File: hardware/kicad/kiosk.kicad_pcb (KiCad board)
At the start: 2 copper layers, 178 x 116 mm, 15 parts, among them J10 TerminalBlock_MaiXu_MX126-5.0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, J11 TerminalBlock_MaiXu_MX126-5.0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, J13 PinSocket_1x09_P2.54mm_Vertic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, J3 PinSocket_1x14_P2.54mm_Vertic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, J4 PinSocket_1x06_P2.54mm_Vertic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, J5 PinHeader_1x04_P2.54mm_Vertic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, J6 PinSocket_1x06_P2.54mm_Vertic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, J7 PinSocket_1x07_P2.54mm_Vertic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, J9 PinHeader_1x03_P2.54mm_Vertic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, U1 ESP32-S3-CAM

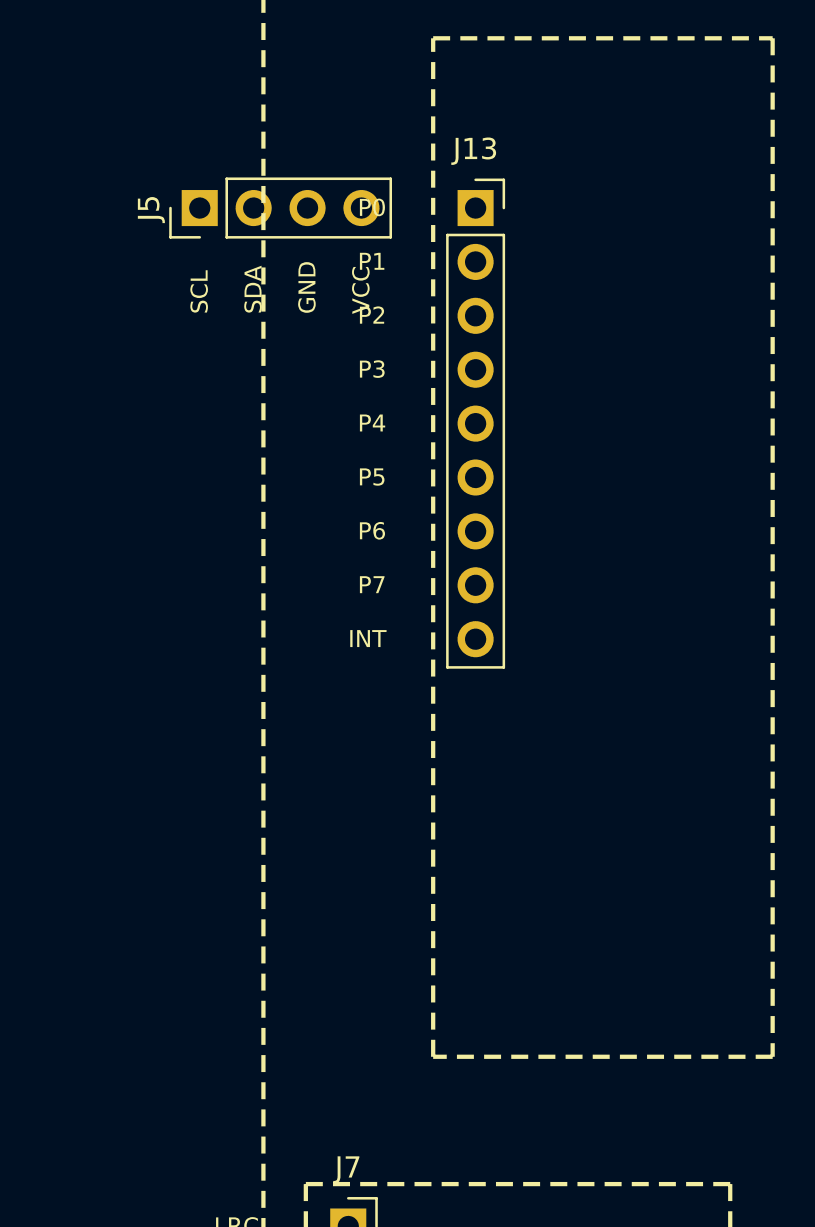
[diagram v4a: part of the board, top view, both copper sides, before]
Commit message: fix(hardware): put the expander's socket and wire holes back the right way
I swapped them last commit on my own reasoning about which row holds the
module better, against what had already been decided: the four supply
pins are soldered pointing down and seat in J5; the port row stays
pointing up and takes wire, stripped and soldered into J13.

J13 keeps all nine holes even though three carry a signal. The six spare
ones cost nothing now and save cutting the board later.

J13 also moves into the gap between the panel and the module, where it
was overlapping the panel's area.
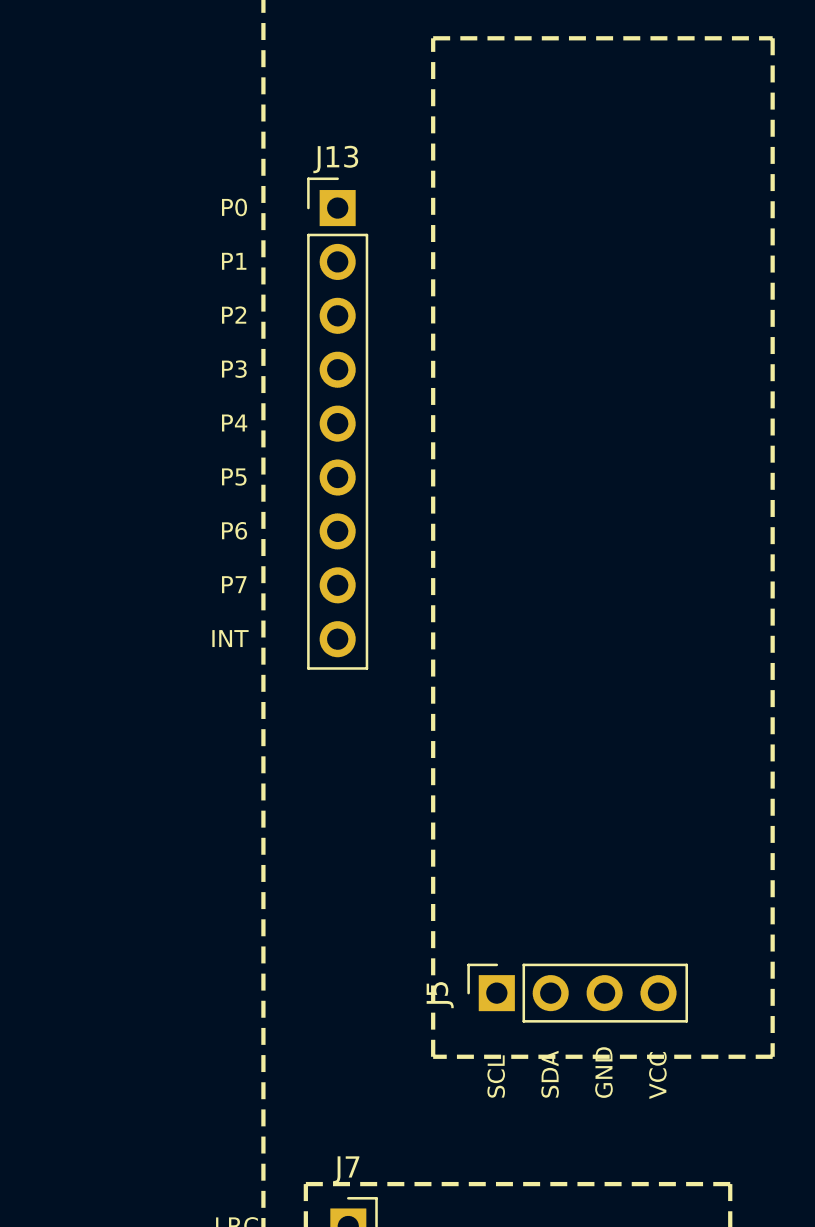
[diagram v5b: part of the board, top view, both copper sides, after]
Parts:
- J13: value PinSocket_1x09_P2.54mm_Vertical -> PinHeader_1x09_P2.54mm_Vertical; footprint Connector_PinSocket_2.54mm:PinSocket_1x09_P2.54mm_Vertical -> Connector_PinHeader_2.54mm:PinHeader_1x09_P2.54mm_Vertical
- J5: value PinHeader_1x04_P2.54mm_Vertical -> PinSocket_1x04_P2.54mm_Vertical; footprint Connector_PinHeader_2.54mm:PinHeader_1x04_P2.54mm_Vertical -> Connector_PinSocket_2.54mm:PinSocket_1x04_P2.54mm_Vertical
- moved J5 39.6 mm to (115.0, 51.0)
- moved J13 6.50 mm to (107.5, 14.0)

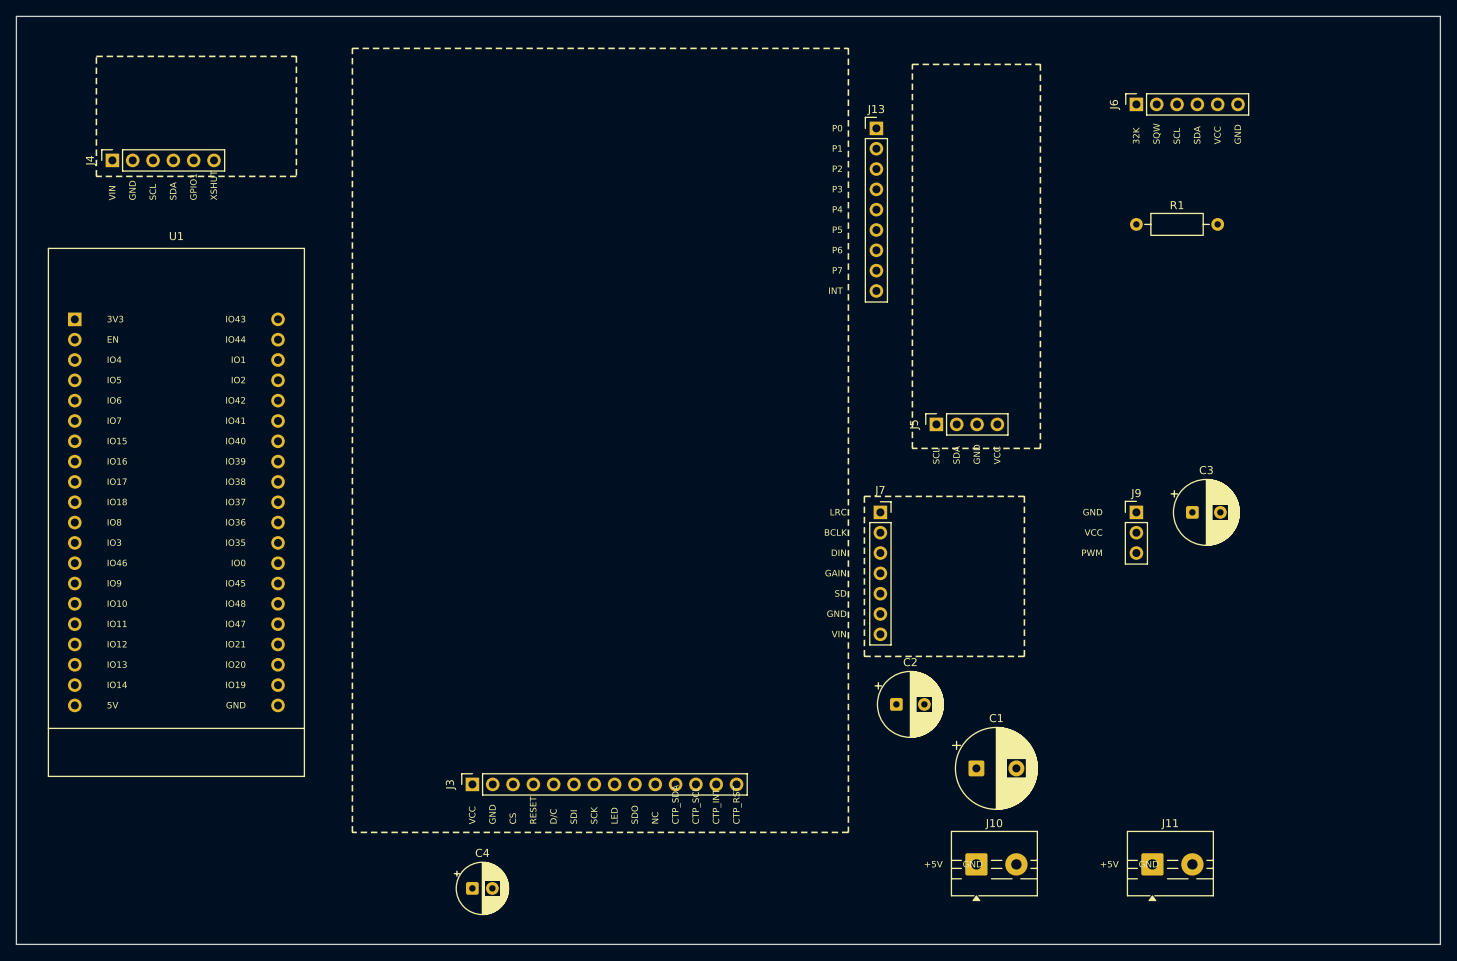
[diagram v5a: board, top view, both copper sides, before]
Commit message: refactor(hardware): square the layout into bands and take back the slack
Parts had been nudged one at a time to clear whatever they last collided
with, and it showed: nothing lined up with anything and the right side had
gaps that were only there because no part had been dropped in them.

Right of the panel is now three bands. The I2C parts above y=54, the two
switching loads between 58 and 80 with a capacitor each, the bulk
capacitor and the two supply terminals below 84. J7 moves to the right
edge of the amplifier's outline so C2 can sit beside it - from the left
edge it was 28 mm away with the module's own body in between.

170 by 116, eight millimetres narrower, with nothing off the board and no
part inside a module's outline.
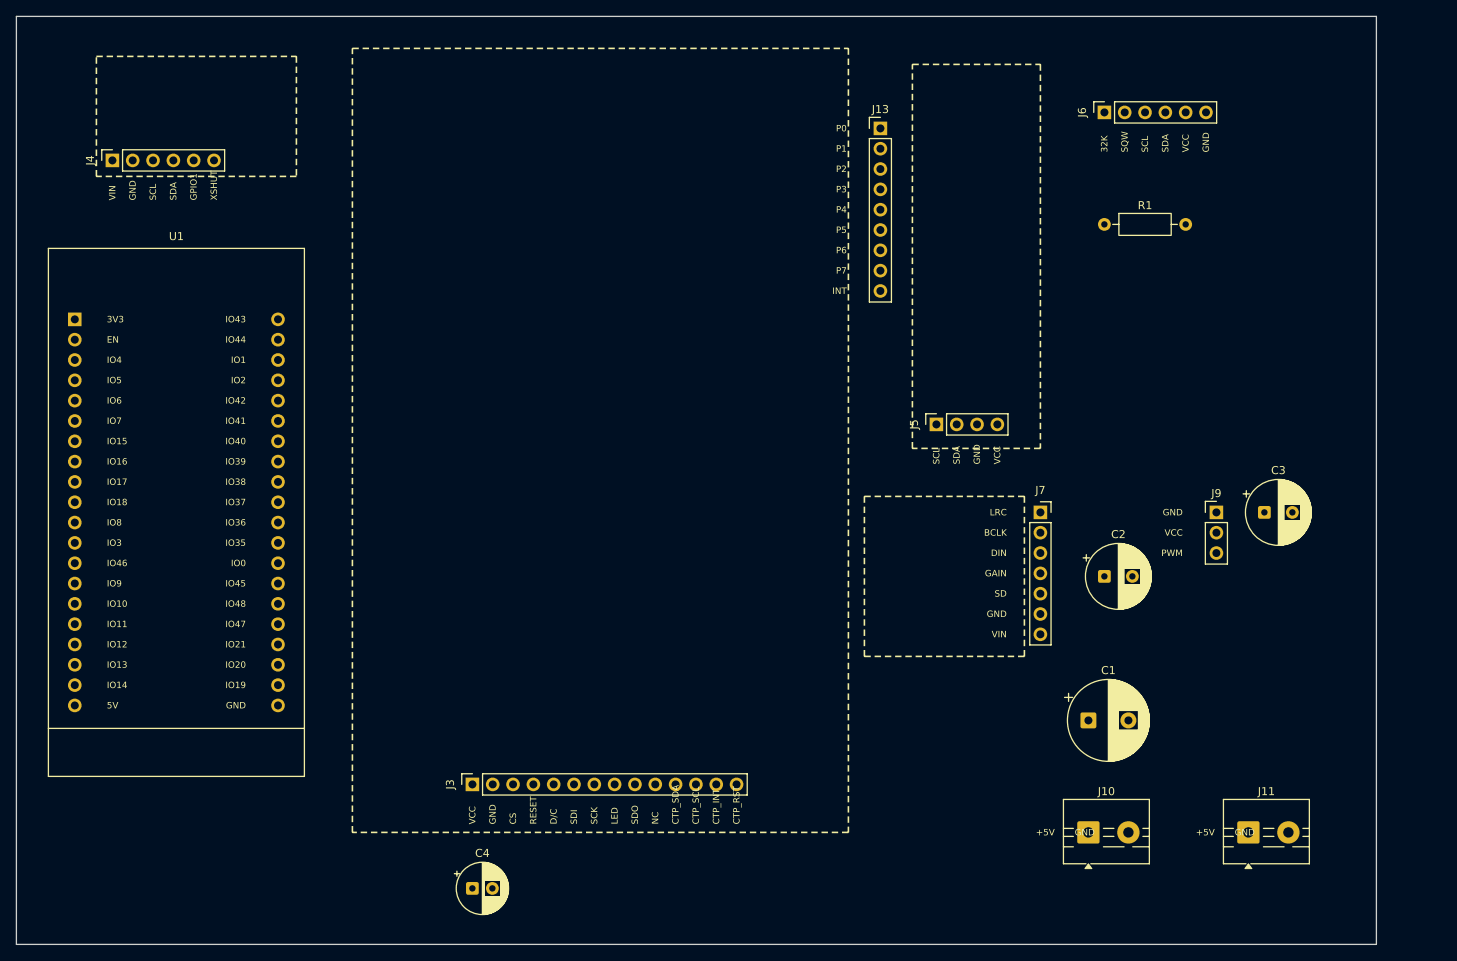
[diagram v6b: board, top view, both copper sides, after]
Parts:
- moved C2 30.5 mm to (136.0, 70.0)
- moved J7 20.0 mm to (128.0, 62.0)
- moved C1 15.2 mm to (134.0, 88.0)
- moved J10 14.6 mm to (134.0, 102.0)
- moved J11 12.6 mm to (154.0, 102.0)
- moved J9 10.0 mm to (150.0, 62.0)
- moved C3 9.00 mm to (156.0, 62.0)
- moved J6 4.12 mm to (136.0, 12.0)
- moved R1 4.00 mm to (136.0, 26.0)
- moved J13 0.50 mm to (108.0, 14.0)
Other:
- board size 178 x 116 mm -> 170 x 116 mm
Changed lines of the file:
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@@
 	(footprint "Connector_PinSocket_2.54mm:PinSocket_1x07_P2.54mm_Vertical"
 		(layer "F.Cu")
-		(at 108 62)
+		(at 128 62)
 		(descr "Through hole straight socket strip, 1x07, 2.54mm pitch, single row (from Kicad 4.0.7), script generated")
 		(tags "Through hole socket strip THT 1x07 2.54mm single row")
@@
 	(footprint "TerminalBlock:TerminalBlock_MaiXu_MX126-5.0-02P_1x02_P5.00mm"
 		(layer "F.Cu")
-		(at 142 106)
+		(at 154 102)
 		(descr "terminal block MaiXu MX126-5.0-02P, 2 pins, pitch 5mm, size 10.5x7.8mm, drill diameter 1.3mm, pad diameter 2.8mm, https://www.lcsc.com/datasheet/lcsc_datasheet_2309150913_MAX-MX126-5-0-03P-GN01-Cu-S-A_C5188435.pdf")
 		(tags "THT terminal block MaiXu MX126-5.0-02P pitch 5mm size 10.5x7.8mm drill 1.3mm pad 2.8mm")
@@
 	(footprint "Capacitor_THT:CP_Radial_D10.0mm_P5.00mm"
 		(layer "F.Cu")
-		(at 120 94)
+		(at 134 88)
 		(descr "CP, Radial series, Radial, pin pitch=5.00mm, diameter=10mm, height=16mm, Electrolytic Capacitor")
 		(tags "CP Radial series Radial pin pitch 5.00mm diameter 10mm height 16mm Electrolytic Capacitor")
@@
 	(footprint "Resistor_THT:R_Axial_DIN0207_L6.3mm_D2.5mm_P10.16mm_Horizontal"
 		(layer "F.Cu")
-		(at 140 26)
+		(at 136 26)
 		(descr "Resistor, Axial_DIN0207 series, Axial, Horizontal, pin pitch=10.16mm, 0.25W = 1/4W, length*diameter=6.3*2.5mm^2, http://cdn-reichelt.de/documents/datenblatt/B400/1_4W%23YAG.pdf")
 		(tags "Resistor Axial_DIN0207 series Axial Horizontal pin pitch 10.16mm 0.25W = 1/4W length 6.3mm diameter 2.5mm")
@@
 	(footprint "Connector_PinHeader_2.54mm:PinHeader_1x03_P2.54mm_Vertical"
 		(layer "F.Cu")
-		(at 140 62)
+		(at 150 62)
 		(descr "Through hole straight pin header, 1x03, 2.54mm pitch, single row")
 		(tags "Through hole pin header THT 1x03 2.54mm single row")
@@
 	(footprint "Connector_PinSocket_2.54mm:PinSocket_1x06_P2.54mm_Vertical"
 		(layer "F.Cu")
-		(at 140 11 90)
+		(at 136 12 90)
 		(descr "Through hole straight socket strip, 1x06, 2.54mm pitch, single row (from Kicad 4.0.7), script generated")
 		(tags "Through hole socket strip THT 1x06 2.54mm single row")
@@
 	(footprint "Connector_PinHeader_2.54mm:PinHeader_1x09_P2.54mm_Vertical"
 		(layer "F.Cu")
-		(at 107.5 14)
+		(at 108 14)
 		(descr "Through hole straight pin header, 1x09, 2.54mm pitch, single row")
 		(tags "Through hole pin header THT 1x09 2.54mm single row")
@@
 	(footprint "TerminalBlock:TerminalBlock_MaiXu_MX126-5.0-02P_1x02_P5.00mm"
 		(layer "F.Cu")
-		(at 120 106)
+		(at 134 102)
 		(descr "terminal block MaiXu MX126-5.0-02P, 2 pins, pitch 5mm, size 10.5x7.8mm, drill diameter 1.3mm, pad diameter 2.8mm, https://www.lcsc.com/datasheet/lcsc_datasheet_2309150913_MAX-MX126-5-0-03P-GN01-Cu-S-A_C5188435.pdf")
 		(tags "THT terminal block MaiXu MX126-5.0-02P pitch 5mm size 10.5x7.8mm drill 1.3mm pad 2.8mm")
@@
 	(footprint "Capacitor_THT:CP_Radial_D8.0mm_P3.50mm"
 		(layer "F.Cu")
-		(at 110 86)
+		(at 136 70)
 		(descr "CP, Radial series, Radial, pin pitch=3.50mm, diameter=8mm, height=12mm, Electrolytic Capacitor")
 		(tags "CP Radial series Radial pin pitch 3.50mm diameter 8mm height 12mm Electrolytic Capacitor")
@@
 	(footprint "Capacitor_THT:CP_Radial_D8.0mm_P3.50mm"
 		(layer "F.Cu")
-		(at 147 62)
+		(at 156 62)
 		(descr "CP, Radial series, Radial, pin pitch=3.50mm, diameter=8mm, height=12mm, Electrolytic Capacitor")
 		(tags "CP Radial series Radial pin pitch 3.50mm diameter 8mm height 12mm Electrolytic Capacitor")
@@
 	(gr_line
 		(start 0 0)
-		(end 178 0)
+		(end 170 0)
 		(stroke
 			(width 0.1)
@@
 	)
 	(gr_line
-		(start 178 0)
-		(end 178 116)
+		(start 170 0)
+		(end 170 116)
 		(stroke
 			(width 0.1)
@@
 	)
 	(gr_line
-		(start 178 116)
+		(start 170 116)
 		(end 0 116)
 		(stroke
@@
 	)
 	(gr_text "P0"
-		(at 103.3 14 0)
+		(at 103.8 14 0)
 		(layer "F.SilkS")
 		(effects
@@
 	)
 	(gr_text "P1"
-		(at 103.3 16.54 0)
+		(at 103.8 16.54 0)
 		(layer "F.SilkS")
 		(effects
@@
 	)
 	(gr_text "P2"
-		(at 103.3 19.08 0)
+		(at 103.8 19.08 0)
 		(layer "F.SilkS")
 		(effects
@@
 	)
 	(gr_text "P3"
-		(at 103.3 21.62 0)
+		(at 103.8 21.62 0)
 		(layer "F.SilkS")
 		(effects
@@
 	)
 	(gr_text "P4"
-		(at 103.3 24.16 0)
+		(at 103.8 24.16 0)
 		(layer "F.SilkS")
 		(effects
@@
 	)
 	(gr_text "P5"
-		(at 103.3 26.7 0)
+		(at 103.8 26.7 0)
 		(layer "F.SilkS")
 		(effects
@@
 	)
 	(gr_text "P6"
-		(at 103.3 29.24 0)
+		(at 103.8 29.24 0)
 		(layer "F.SilkS")
 		(effects
@@
 	)
 	(gr_text "P7"
-		(at 103.3 31.78 0)
+		(at 103.8 31.78 0)
 		(layer "F.SilkS")
 		(effects
@@
 	)
 	(gr_text "INT"
-		(at 103.3 34.32 0)
+		(at 103.8 34.32 0)
 		(layer "F.SilkS")
 		(effects
@@
 	)
 	(gr_text "LRC"
-		(at 103.8 62 0)
+		(at 123.8 62 0)
 		(layer "F.SilkS")
 		(effects
@@
 	)
 	(gr_text "BCLK"
-		(at 103.8 64.54 0)
+		(at 123.8 64.54 0)
 		(layer "F.SilkS")
 		(effects
@@
 	)
 	(gr_text "DIN"
-		(at 103.8 67.08 0)
+		(at 123.8 67.08 0)
 		(layer "F.SilkS")
 		(effects
@@
 	)
 	(gr_text "GAIN"
-		(at 103.8 69.62 0)
+		(at 123.8 69.62 0)
 		(layer "F.SilkS")
 		(effects
@@
 	)
 	(gr_text "SD"
-		(at 103.8 72.16 0)
+		(at 123.8 72.16 0)
 		(layer "F.SilkS")
 		(effects
@@
 	)
 	(gr_text "GND"
-		(at 103.8 74.7 0)
+		(at 123.8 74.7 0)
 		(layer "F.SilkS")
 		(effects
@@
 	)
 	(gr_text "VIN"
-		(at 103.8 77.24 0)
+		(at 123.8 77.24 0)
 		(layer "F.SilkS")
 		(effects
@@
 	)
 	(gr_text "+5V"
-		(at 115.8 106 0)
+		(at 129.8 102 0)
 		(layer "F.SilkS")
 		(effects
@@
 	)
 	(gr_text "GND"
-		(at 120.8 106 0)
+		(at 134.8 102 0)
 		(layer "F.SilkS")
 		(effects
@@
 	)
 	(gr_text "GND"
-		(at 135.8 62 0)
+		(at 145.8 62 0)
 		(layer "F.SilkS")
 		(effects
@@
 	)
 	(gr_text "VCC"
-		(at 135.8 64.54 0)
+		(at 145.8 64.54 0)
 		(layer "F.SilkS")
 		(effects
@@
 	)
 	(gr_text "PWM"
-		(at 135.8 67.08 0)
+		(at 145.8 67.08 0)
 		(layer "F.SilkS")
 		(effects
@@
 	)
 	(gr_text "+5V"
-		(at 137.8 106 0)
+		(at 149.8 102 0)
 		(layer "F.SilkS")
 		(effects
@@
 	)
 	(gr_text "GND"
-		(at 142.8 106 0)
+		(at 154.8 102 0)
 		(layer "F.SilkS")
 		(effects
@@
 	)
 	(gr_text "32K"
-		(at 140 16 90)
+		(at 136 17 90)
 		(layer "F.SilkS")
 		(effects
@@
 	)
 	(gr_text "SQW"
-		(at 142.54 16 90)
+		(at 138.54 17 90)
 		(layer "F.SilkS")
 		(effects
@@
 	)
 	(gr_text "SCL"
-		(at 145.08 16 90)
+		(at 141.08 17 90)
 		(layer "F.SilkS")
 		(effects
@@
 	)
 	(gr_text "SDA"
-		(at 147.62 16 90)
+		(at 143.62 17 90)
 		(layer "F.SilkS")
 		(effects
@@
 	)
 	(gr_text "VCC"
-		(at 150.16 16 90)
+		(at 146.16 17 90)
 		(layer "F.SilkS")
 		(effects
@@
 	)
 	(gr_text "GND"
-		(at 152.7 16 90)
+		(at 148.7 17 90)
 		(layer "F.SilkS")
 		(effects
